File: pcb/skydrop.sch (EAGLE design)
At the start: 99 parts, among them IC1 RT9193-33GB, IC2 MCP73831/OT, IC3 STM809SWX6F, IC4 MS5611-01BA03, Q1 BSS84, Q10 BSS84, Q2 BSS123, Q3 BSS123, Q4 BSS84, Q5 BSS84, Q6 BSS84, Q7 BSS123, Q8 BSS84, Q9 BSS84, U2 W25Q16BVSS

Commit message: improve pcb
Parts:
- removed R20: 100k, skydrop:R_0805
- removed R42: 47k, skydrop:R_0805
- added SD1: TF-HOLDER, skydrop:TF-HOLDER
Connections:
- removed net BTN_C_B1: C22.1, R42.1
- removed net N$40: J1.USBID, R20.1
- net GND: no longer R20.2, R42.2
- net USB_VBUS: now also C22.1
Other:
- moved on the sheet: C16, C22, D3, D4, R40, R41, R43

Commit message: [pcb] new display
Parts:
- removed C, L, R: DTSM-6, skydrop:DTSM-6
- removed C7: (no value), skydrop:C_1206
- removed LCD1: LPH-7366, skydrop:LPH-7366
- removed Q4: BSS84, transistor-small-signal:BSS84
- removed R21: 100, skydrop:R_0805
- removed SD1: TF-HOLDER, skydrop:TF-HOLDER
- added BTN_C, BTN_L, BTN_R: TS-1109-7, skydrop:DIP-BUTTON-TOP-BLACK(4P-D6.2MM)
- added C23, C24, C25, C6: 1uf, skydrop:C_0805
- added C26: 3.3uf, skydrop:C_0805
- added C27: 0.1uf, skydrop:C_0805
- added C28: 10uf, skydrop:C_0805
- added U$1: NOKIA5110, skydrop:NOKIA5110
- R19: value 10k -> 0; device skydrop:R_0805 -> skydrop:R_1206
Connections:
- removed net N$26: Q4.G, R19.1, R21.1
- new net N$15: C27.2, C28.2, R19.2, U$1.DB0, U$1.DB1, U$1.DB2, U$1.DB3, U$1.DB4, U$1.DB5, U$1.E_RD, U$1.OSC1, U$1.PS1, U$1.R/W(WR), U$1.VDD
- new net N$40: C6.2, U$1.V1
- new net N$47: C23.2, U$1.V2
- new net N$48: C24.2, U$1.V3
- new net N$49: C25.2, U$1.V4
- new net N$50: C26.2, U$1.VOUT
- new net N$52: BTN_R.B0
- net BTN_C_T: now also BTN_C.B1; no longer C.2
- net BTN_L_T: now also BTN_L.B1; no longer L.2
- net BTN_R_T: now also BTN_R.B1; no longer R.2
- net GND_T: now also C23.1, C24.1, C25.1, C26.1, C27.1, C28.1, C6.1, U$1.PS0, U$1.PS2, U$1.VSS; no longer C7.1, LCD1.GND
- net LCD_CE_T: now also U$1.CSB; no longer LCD1./SCE
- net LCD_CLK_T: now also U$1.DB6; no longer LCD1.SCLK
- net LCD_DC_T: now also U$1.A0; no longer LCD1.D/C
- net LCD_DIN_T: now also U$1.DB7; no longer LCD1.SDIN
- net LCD_PWR_T: no longer R21.2
- net LCD_RST_T: now also U$1./RES; no longer LCD1./RES
- net N$25: now also BTN_L.B0; no longer LCD1.OSC, LCD1.VDD, Q4.D
- net N$36: now also BTN_C.B0; no longer C7.2, LCD1.VOUT
- net VCC_T: now also BTN_C.A0, BTN_C.A1, BTN_L.A0, BTN_L.A1, BTN_R.A0, BTN_R.A1, R19.1; no longer C.4, L.4, Q4.S, R.4, R19.2
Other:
- moved on the sheet: R19

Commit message: improve pcb for new display
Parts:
- C1, C15, C2, C4: device skydrop:C_1210 -> skydrop:C_0805
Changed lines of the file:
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@@
 <setting verticaltext="up"/>
 </settings>
-<grid distance="0.1" unitdist="inch" unit="inch" style="lines" multiple="1" display="yes" altdistance="0.01" altunitdist="inch" altunit="inch"/>
+<grid distance="0.1" unitdist="inch" unit="inch" style="lines" multiple="1" display="no" altdistance="0.01" altunitdist="inch" altunit="inch"/>
 <layers>
 <layer number="1" name="Top" color="4" fill="1" visible="no" active="no"/>
@@
 <part name="IC2" library="skydrop" deviceset="MCP73831" device="/OT"/>
 <part name="R1" library="skydrop" deviceset="R_" device="0805" value="6.8k"/>
-<part name="C1" library="skydrop" deviceset="C_" device="1210"/>
-<part name="C2" library="skydrop" deviceset="C_" device="1210"/>
+<part name="C1" library="skydrop" deviceset="C_" device="0805"/>
+<part name="C2" library="skydrop" deviceset="C_" device="0805"/>
 <part name="P+2" library="supply1" deviceset="+5V" device=""/>
 <part name="SUPPLY1" library="supply2" deviceset="+UB" device=""/>
@@
 <part name="IC3" library="skydrop" deviceset="TCM809" device="" value="STM809SWX6F"/>
 <part name="C3" library="skydrop" deviceset="C_" device="0805"/>
-<part name="C4" library="skydrop" deviceset="C_" device="1210"/>
+<part name="C4" library="skydrop" deviceset="C_" device="0805"/>
 <part name="C5" library="skydrop" deviceset="C_" device="0805" value="22nf"/>
 <part name="Q1" library="transistor-small-signal" deviceset="BSS84" device=""/>
@@
 <part name="J1" library="skydrop" deviceset="USB-AB" device=""/>
 <part name="C11" library="skydrop" deviceset="C_" device="0805"/>
-<part name="C15" library="skydrop" deviceset="C_" device="1210"/>
+<part name="C15" library="skydrop" deviceset="C_" device="0805"/>
 <part name="GND28" library="supply1" deviceset="GND" device=""/>
 <part name="R2" library="skydrop" deviceset="R_" device="1206" value="0"/>

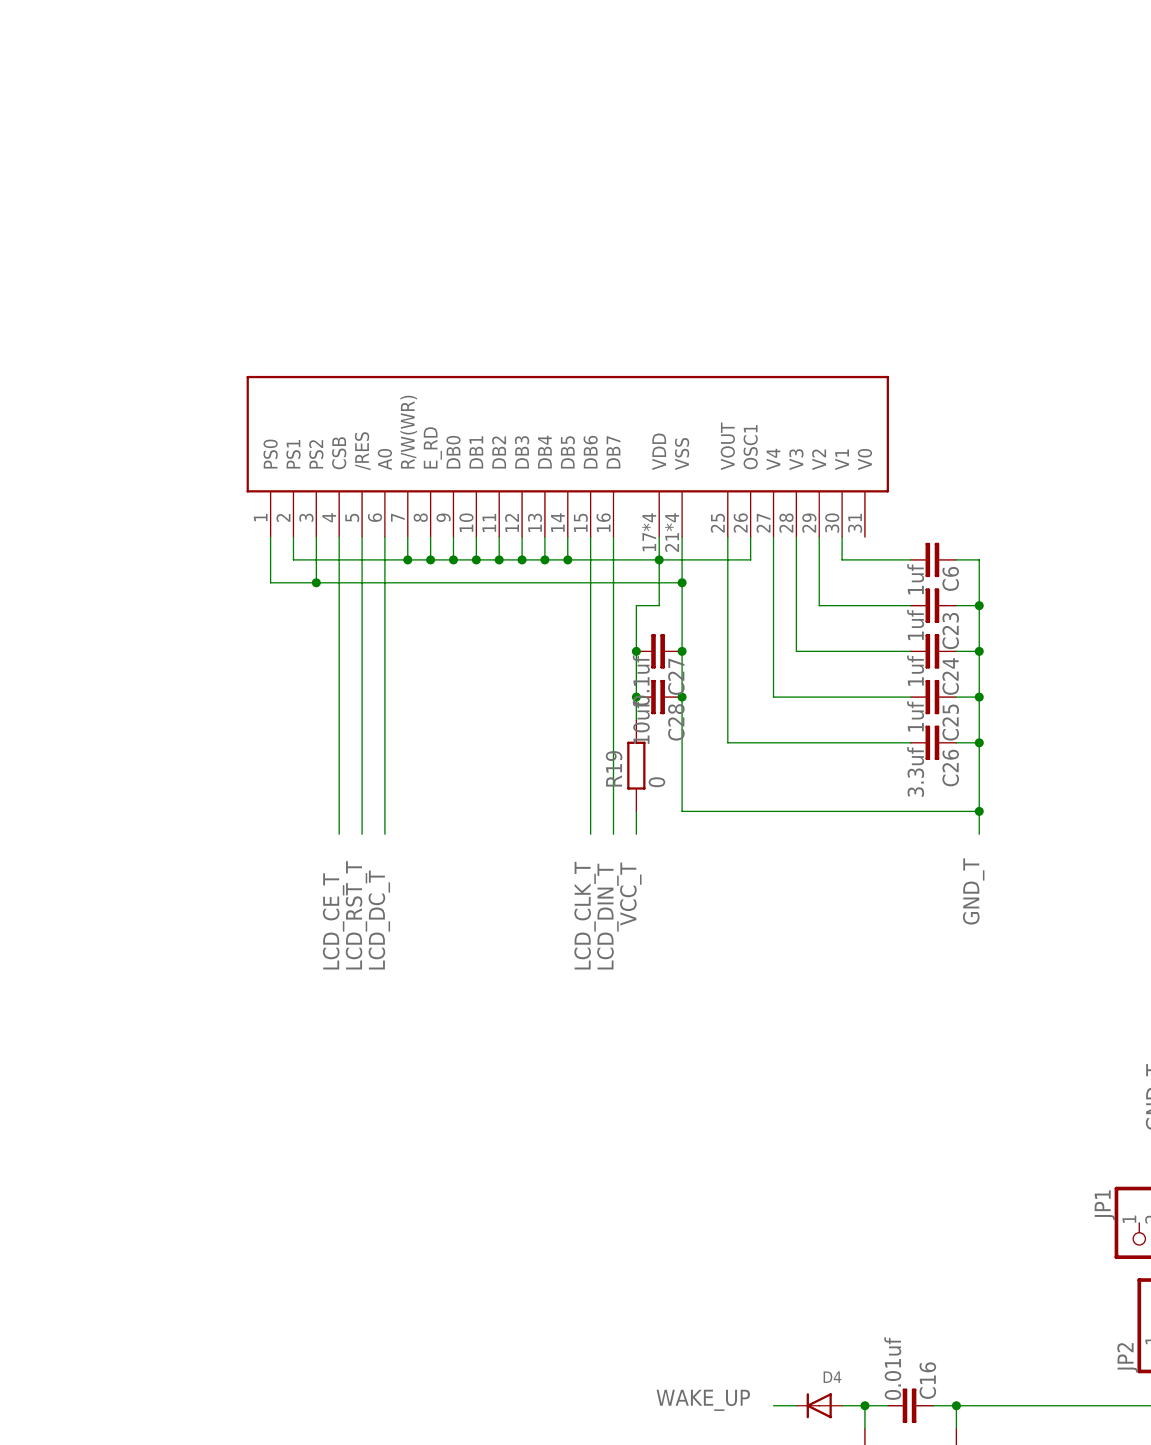
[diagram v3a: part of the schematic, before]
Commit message: add spi extender
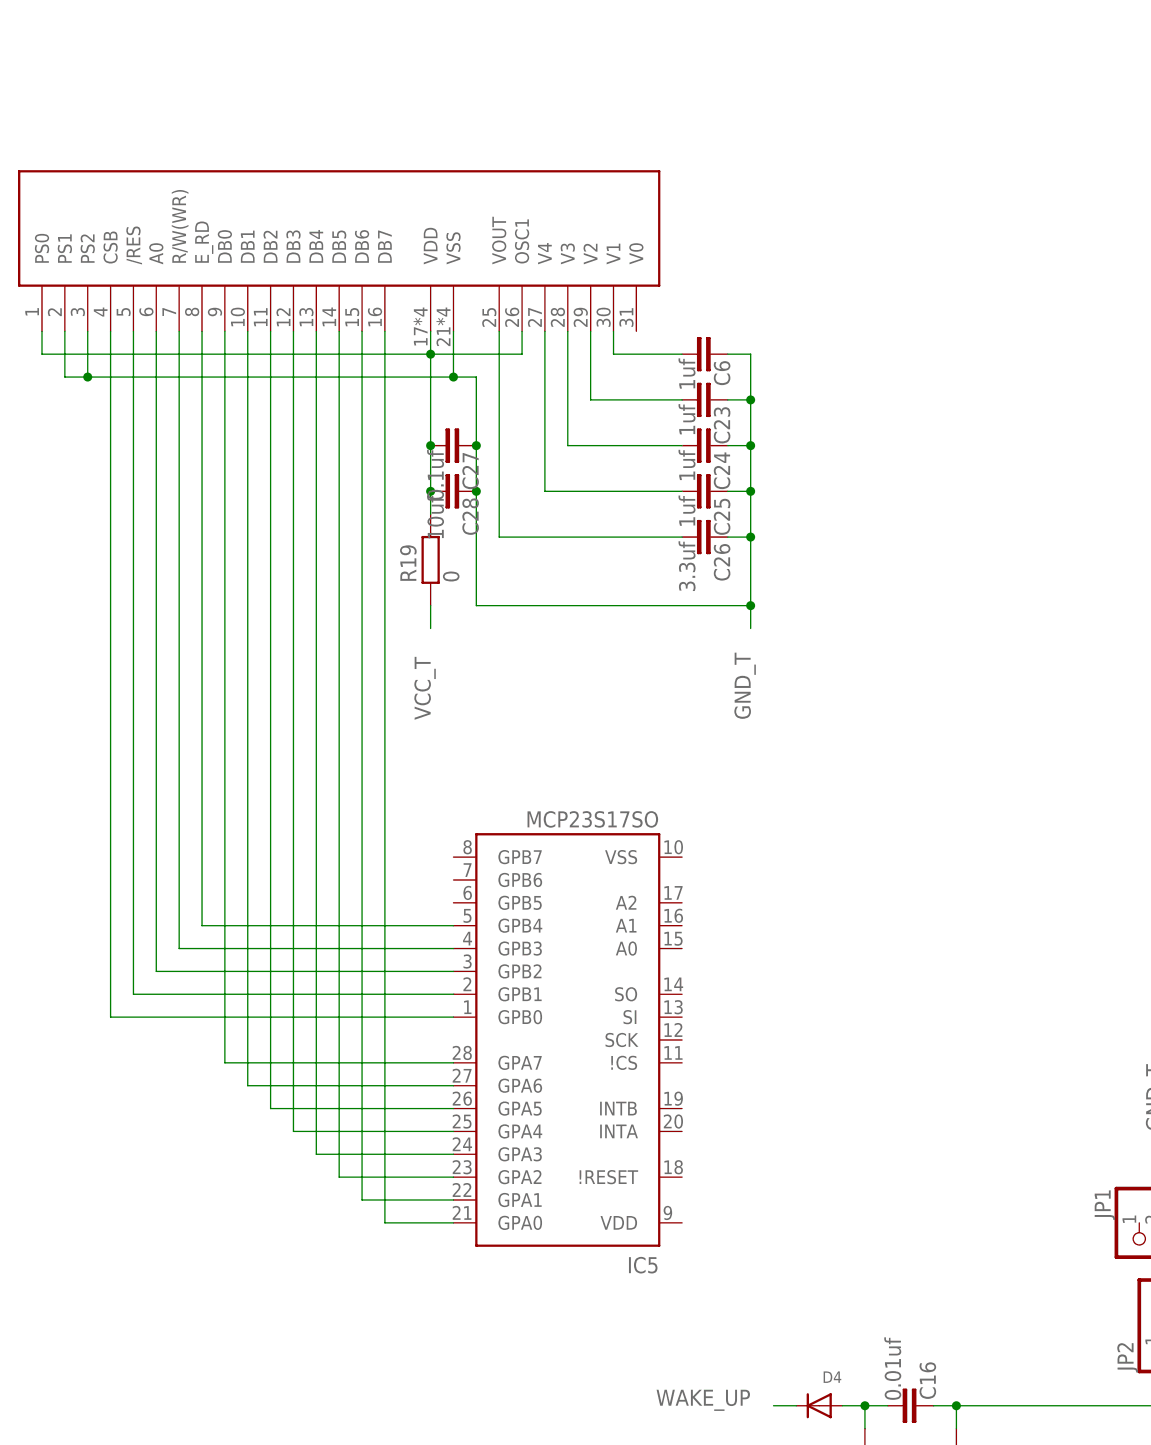
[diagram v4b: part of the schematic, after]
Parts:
- added IC5: MCP23S17SO, skydrop:MCP23S17SO
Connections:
- new net N$51: IC5.GPA7, U$1.DB0
- new net N$53: IC5.GPA6, U$1.DB1
- new net N$54: IC5.GPA5, U$1.DB2
- new net N$55: IC5.GPA4, U$1.DB3
- new net N$56: IC5.GPA3, U$1.DB4
- new net N$57: IC5.GPA2, U$1.DB5
- new net N$58: IC5.GPA1, U$1.DB6
- new net N$59: IC5.GPA0, U$1.DB7
- new net N$60: IC5.GPB0, U$1.CSB
- new net N$61: IC5.GPB1, U$1./RES
- new net N$62: IC5.GPB2, U$1.A0
- new net N$63: IC5.GPB3, U$1.R/W(WR)
- new net N$64: IC5.GPB4, U$1.E_RD
- net GND_T: now also U$1.PS1; no longer U$1.PS0
- net LCD_CE_T: no longer U$1.CSB
- net LCD_CLK_T: no longer U$1.DB6
- net LCD_DC_T: no longer U$1.A0
- net LCD_DIN_T: no longer U$1.DB7
- net LCD_RST_T: no longer U$1./RES
- net N$15: now also U$1.PS0; no longer U$1.DB0, U$1.DB1, U$1.DB2, U$1.DB3, U$1.DB4, U$1.DB5, U$1.E_RD, U$1.PS1, U$1.R/W(WR)
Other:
- moved on the sheet: C23, C24, C25, C26, C27, C28, C6, R19

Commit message: improove spi extender
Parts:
- added R20: 0, skydrop:R_1206
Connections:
- removed net LCD_DC_B: JP2.3, UC1.PC5/ADC15
- removed net LCD_DC_T: JP1.4
- removed net LCD_PWR_B: JP2.4, UC1.PC4/ADC14
- removed net LCD_PWR_T: JP1.5
- new net LCD_DOUT_B: JP2.6, UC1.PA6/SPI1_MISO/ADC6/TIM3_CH1
- new net LCD_DOUT_T: IC5.SO, JP1.7
- new net N$65: R20.2, U$1.PS1, U$1.PS2
- net GND_T: now also IC5.A0, IC5.A1, IC5.A2, IC5.VSS; no longer U$1.PS1, U$1.PS2
- net LCD_CE_B: now also JP2.4, UC1.PC4/ADC14; no longer JP2.2, UC1.PB0/ADC8/TIM3_CH3
- net LCD_CE_T: now also IC5.\!CS, JP1.5; no longer JP1.3
- net LCD_CLK_B: now also JP2.7; no longer JP2.6
- net LCD_CLK_T: now also IC5.SCK, JP1.8; no longer JP1.7
- net LCD_DIN_T: now also IC5.SI
- net LCD_RST_B: now also JP2.3, UC1.PC5/ADC15; no longer JP2.7, UC1.PA4/SPI1_NSS/USART2_CK/ADC4
- net LCD_RST_T: now also IC5.\!RESET, JP1.4; no longer JP1.8
- net VCC_T: now also IC5.VDD

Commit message: [pcb] improove
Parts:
- added Q4: BSS123, transistor-small-signal:BSS123
- added R21: 100k, skydrop:R_0805
- added R42: 10k, skydrop:R_0805
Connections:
- removed net N$25: BTN_L.B0
- removed net N$36: BTN_C.B0
- removed net N$52: BTN_R.B0
- new net LCD_PWM_B: JP2.3, UC1.PB0/ADC8/TIM3_CH3
- new net LCD_PWM_T: JP1.4, Q4.G, R42.1
- new net N$26: Q4.D, U$1.K
- net BTN_C_T: now also BTN_C.B0, JP1.10; no longer JP1.12
- net BTN_L_T: now also BTN_L.B0
- net BTN_R_T: now also BTN_R.B0, JP1.12; no longer JP1.10
- net GND_T: now also Q4.S, R20.1, R21.2, R42.2
- net LCD_CE_B: now also JP2.8, UC1.PA4/SPI1_NSS/USART2_CK/ADC4; no longer JP2.4, UC1.PC4/ADC14
- net LCD_CE_T: now also JP1.9; no longer JP1.5
- net LCD_RST_B: now also JP2.4, UC1.PC4/ADC14; no longer JP2.3, UC1.PC5/ADC15
- net LCD_RST_T: now also JP1.5, R19.1; no longer IC5.\!RESET, JP1.4
- net N$15: now also IC5.\!RESET, R21.1; no longer C27.2, C28.2, U$1.OSC1, U$1.PS0, U$1.VDD
- net VCC: now also JP2.2; no longer JP2.8
- net VCC_T: now also C27.2, C28.2, JP1.3, U$1.A, U$1.OSC1, U$1.PS0, U$1.VDD; no longer JP1.9, R19.1
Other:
- moved on the sheet: BTN_C, BTN_L, BTN_R, C16, C23, C24, C25, C26, C27, C28, C6, D4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

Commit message: [pcb] improve
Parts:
- removed BUT: BUT, SparkFun_20110922_my:SWITCH-MOMENTARY-2-SMD-1101NE
- added SW1: 431256083736, skydrop:431256083736
- added U$2: MPU-9250, invensense:MPU-9250
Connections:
- removed net OSC32_IN_3: C19.2, OSC2.1, UC1.PC14/OSC32_IN
- removed net OSC32_OUT_4: C20.2, OSC2.2, UC1.PC15/OSC_OUT
- new net N$25: C19.2, OSC2.2, UC1.PC14/OSC32_IN
- new net N$36: C20.2, OSC2.1, UC1.PC15/OSC_OUT
- net GND: now also SW1.2; no longer BUT.2
- net N$11: now also SW1.3; no longer BUT.1
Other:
- moved on the sheet: OSC2
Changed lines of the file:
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@@
 <setting verticaltext="up"/>
 </settings>
-<grid distance="0.1" unitdist="inch" unit="inch" style="lines" multiple="1" display="no" altdistance="0.01" altunitdist="inch" altunit="inch"/>
+<grid distance="0.05" unitdist="inch" unit="inch" style="lines" multiple="1" display="yes" altdistance="0.01" altunitdist="inch" altunit="inch"/>
 <layers>
 <layer number="1" name="Top" color="4" fill="1" visible="no" active="no"/>
@@
 <layer number="56" name="wert" color="7" fill="1" visible="no" active="no"/>
 <layer number="57" name="tCAD" color="7" fill="1" visible="no" active="no"/>
+<layer number="58" name="bCAD" color="7" fill="1" visible="no" active="no"/>
 <layer number="59" name="tCarbon" color="7" fill="1" visible="no" active="no"/>
 <layer number="60" name="bCarbon" color="7" fill="1" visible="no" active="no"/>
@@
 <part name="R16" library="skydrop" deviceset="R_" device="0805" value="10k"/>
 <part name="GND29" library="SparkFun" deviceset="GND" device=""/>
-<part name="BUT" library="SparkFun_20110922_my" deviceset="SWITCH-MOMENTARY-2" device="-SMD-1101NE" value="BUT"/>
 <part name="GND40" library="SparkFun" deviceset="GND" device=""/>
 <part name="C19" library="skydrop" deviceset="C_" device="0805" value="18pF"/>
@@
 <part name="R27" library="skydrop" deviceset="R_" device="0805" value="100"/>
 <part name="R29" library="skydrop" deviceset="R_" device="0805" value="100"/>
-<part name="GND20" library="SparkFun" deviceset="GND" device=""/>
 <part name="R24" library="skydrop" deviceset="R_" device="0805" value="22"/>
 <part name="R30" library="skydrop" deviceset="R_" device="0805" value="22"/>
@@
 <part name="Q4" library="transistor-small-signal" deviceset="BSS123" device=""/>
 <part name="R42" library="skydrop" deviceset="R_" device="0805" value="10k"/>
+<part name="SW1" library="skydrop" deviceset="431256083736" device=""/>
+<part name="GND35" library="SparkFun" deviceset="GND" device=""/>
+<part name="U$2" library="invensense" deviceset="MPU-9250" device=""/>
 </parts>
 <sheets>
@@
 <instance part="R16" gate="G$1" x="137.16" y="-101.6" rot="R180"/>
 <instance part="GND29" gate="1" x="-96.52" y="96.52" rot="MR0"/>
-<instance part="BUT" gate="G$1" x="-68.58" y="-139.7" rot="MR0"/>
 <instance part="GND40" gate="1" x="160.02" y="-186.69" rot="MR0"/>
 <instance part="C19" gate="G$1" x="154.94" y="-175.26" smashed="yes" rot="R270">
@@
 <attribute name="VALUE" x="-31.623" y="-128.27" size="1.778" layer="96" rot="R90"/>
 </instance>
-<instance part="OSC2" gate="G$1" x="147.32" y="-177.8" rot="R270"/>
+<instance part="OSC2" gate="G$1" x="147.32" y="-177.8" rot="R90"/>
 <instance part="JP1" gate="G$1" x="-157.48" y="-17.78" rot="MR270"/>
 <instance part="GND1" gate="1" x="-180.34" y="-45.72"/>
@@
 <instance part="R27" gate="G$1" x="-114.3" y="-200.66" rot="MR0"/>
 <instance part="R29" gate="G$1" x="-185.42" y="-200.66" rot="MR0"/>
-<instance part="GND20" gate="1" x="-76.2" y="-154.94"/>
 <instance part="R24" gate="G$1" x="-60.96" y="116.84" rot="R180"/>
 <instance part="R30" gate="G$1" x="-60.96" y="124.46" rot="R180"/>
@@
 <attribute name="VALUE" x="-215.9" y="108.585" size="1.778" layer="96" rot="MR0"/>
 </instance>
+<instance part="SW1" gate="G$1" x="-78.74" y="-143.51"/>
+<instance part="GND35" gate="1" x="-69.85" y="-154.94"/>
+<instance part="U$2" gate="G$1" x="217.17" y="-205.74"/>
 </instances>
 <busses>
@@
 <pinref part="OSC" gate="G$1" pin="1"/>
 <pinref part="C13" gate="G$1" pin="2"/>
-</segment>
-</net>
-<net name="OSC32_IN_3" class="0">
-<segment>
-<wire x1="152.4" y1="-175.26" x2="147.32" y2="-175.26" width="0.1524" layer="91"/>
-<junction x="147.32" y="-175.26"/>
-<pinref part="C19" gate="G$1" pin="2"/>
-<pinref part="OSC2" gate="G$1" pin="1"/>
-<pinref part="UC1" gate="G$1" pin="PC14/OSC32_IN"/>
-<wire x1="147.32" y1="-175.26" x2="104.14" y2="-175.26" width="0.1524" layer="91"/>
-</segment>
-</net>
-<net name="OSC32_OUT_4" class="0">
-<segment>
-<pinref part="UC1" gate="G$1" pin="PC15/OSC_OUT"/>
-<wire x1="152.4" y1="-180.34" x2="147.32" y2="-180.34" width="0.1524" layer="91"/>
-<junction x="147.32" y="-180.34"/>
-<pinref part="C20" gate="G$1" pin="2"/>
-<pinref part="OSC2" gate="G$1" pin="2"/>
-<wire x1="147.32" y1="-180.34" x2="142.24" y2="-180.34" width="0.1524" layer="91"/>
-<wire x1="142.24" y1="-180.34" x2="142.24" y2="-177.8" width="0.1524" layer="91"/>
-<wire x1="104.14" y1="-177.8" x2="142.24" y2="-177.8" width="0.1524" layer="91"/>
 </segment>
 </net>
@@
 </segment>
 <segment>
-<pinref part="BUT" gate="G$1" pin="2"/>
-<pinref part="GND20" gate="1" pin="GND"/>
-<wire x1="-76.2" y1="-152.4" x2="-76.2" y2="-139.7" width="0.1524" layer="91"/>
-<wire x1="-76.2" y1="-139.7" x2="-73.66" y2="-139.7" width="0.1524" layer="91"/>
-</segment>
-<segment>
 <pinref part="R32" gate="G$1" pin="2"/>
 <pinref part="GND21" gate="1" pin="GND"/>
@@
 <pinref part="GND34" gate="1" pin="GND"/>
 <wire x1="-27.94" y1="114.3" x2="-27.94" y2="119.38" width="0.1524" layer="91"/>
+</segment>
+<segment>
+<pinref part="SW1" gate="G$1" pin="2"/>
+<pinref part="GND35" gate="1" pin="GND"/>
+<wire x1="-76.2" y1="-147.32" x2="-69.85" y2="-147.32" width="0.1524" layer="91"/>
+<wire x1="-69.85" y1="-147.32" x2="-69.85" y2="-152.4" width="0.1524" layer="91"/>
 </segment>
 </net>
@@
 <pinref part="UC1" gate="G$1" pin="NRST"/>
 <wire x1="15.24" y1="-139.7" x2="-58.42" y2="-139.7" width="0.1524" layer="91"/>
-<pinref part="BUT" gate="G$1" pin="1"/>
-<wire x1="-63.5" y1="-139.7" x2="-58.42" y2="-139.7" width="0.1524" layer="91"/>
 <junction x="-58.42" y="-139.7"/>
 <pinref part="C8" gate="G$1" pin="2"/>
 <wire x1="-58.42" y1="-142.24" x2="-58.42" y2="-139.7" width="0.1524" layer="91"/>
+<pinref part="SW1" gate="G$1" pin="3"/>
+<wire x1="-58.42" y1="-139.7" x2="-76.2" y2="-139.7" width="0.1524" layer="91"/>
 </segment>
 </net>
@@
 </segment>
 </net>
+<net name="N$25" class="0">
+<segment>
+<pinref part="UC1" gate="G$1" pin="PC14/OSC32_IN"/>
+<pinref part="OSC2" gate="G$1" pin="2"/>
+<wire x1="104.14" y1="-175.26" x2="147.32" y2="-175.26" width="0.1524" layer="91"/>
+<pinref part="C19" gate="G$1" pin="2"/>
+<wire x1="147.32" y1="-175.26" x2="152.4" y2="-175.26" width="0.1524" layer="91"/>
+<junction x="147.32" y="-175.26"/>
+</segment>
+</net>
+<net name="N$36" class="0">
+<segment>
+<pinref part="C20" gate="G$1" pin="2"/>
+<pinref part="OSC2" gate="G$1" pin="1"/>
+<wire x1="152.4" y1="-180.34" x2="147.32" y2="-180.34" width="0.1524" layer="91"/>
+<wire x1="147.32" y1="-180.34" x2="142.24" y2="-180.34" width="0.1524" layer="91"/>
+<wire x1="142.24" y1="-180.34" x2="142.24" y2="-177.8" width="0.1524" layer="91"/>
+<pinref part="UC1" gate="G$1" pin="PC15/OSC_OUT"/>
+<wire x1="142.24" y1="-177.8" x2="104.14" y2="-177.8" width="0.1524" layer="91"/>
+<junction x="147.32" y="-180.34"/>
+</segment>
+</net>

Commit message: [pcb] improve
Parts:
- added C29, C30: 0.1uF, skydrop:C_0805
- added C7: 10nF, skydrop:C_0805
- added R44, R45: 4.7k, skydrop:R_0805
- R17, R18: value 4.7k -> 0; device skydrop:R_0805 -> skydrop:R_1206
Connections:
- removed net MS5611_VCC: C18.1, IC4.CSB@1, IC4.CSB@2, IC4.PS, IC4.VDD, R17.2, R18.2, UC1.PB5/I2C1_SMBA
- new net N$66: C29.1, U$2.REGOUT
- new net SENS_PWR: C18.1, C30.1, C7.1, IC4.CSB@1, IC4.CSB@2, IC4.PS, IC4.VDD, R44.2, R45.2, U$2.NCS, U$2.RESV, U$2.VDD, U$2.VDDIO, UC1.PB5/I2C1_SMBA
- new net SENS_SCL: R18.1, R45.1, U$2.SCL/SCLK, UC1.PB6/I2C1_SCL/TIM4_CH1
- new net SENS_SDA: R17.1, R44.1, U$2.SDA/SDI, UC1.PB7/I2C1_SDA/TIM4_CH2
- net GND: now also C29.2, C30.2, C7.2, U$2.ADO/SDO, U$2.FSYNC, U$2.GND, U$2.RESV2
- net MS5611_SCL: now also R18.2, U$2.AUX_CL; no longer R17.1, UC1.PB6/I2C1_SCL/TIM4_CH1
- net MS5611_SDA: now also R17.2, U$2.AUX_DA; no longer R18.1, UC1.PB7/I2C1_SDA/TIM4_CH2
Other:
- moved on the sheet: C18, IC4, R17, R18, U$2
